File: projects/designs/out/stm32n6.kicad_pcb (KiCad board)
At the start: 2 copper layers, 89 parts, among them SW1 0R

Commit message: Update designs: add sub-block modules, board definition, layout, and KiCad exports
- Add charger (MCP73831), buck-boost (TPS63806), and LDO (LP5907) sub-block modules
- Add MCP73831 component definition
- Add stm32n6-board.sexp board definition with outline, rules, stackup, and zones
- Add stm32n6.layout with component placements and trace routing
- Mark optional ports on lt3045 module and stm32n6 ADC section
- Update BOM files with resolved component identities
- Add KiCad PCB exports for lt3045, power-6v, and tpsm84338
- Update stm32n6 KiCad PCB with traces, vias, and zone data
- Update footprint courtyard definitions

Co-Authored-By: Claude Opus 4.6 (1M context) <noreply@anthropic.com>
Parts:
- removed C1, C2, C21, C22, C23, C24, C25, C26, C27, C28, C29, C3, C30, C31, C32, C33, C34, C4, C5: 100nF, C_0201_0603Metric
- removed C10, C11, C12, C13, C14, C15, C16, C19, C20: 1uF, C_0201_0603Metric
- removed C17: 10uF, C_0603_1608Metric
- removed the C18 at (240.0, 0.00)
- removed the C18 at (180.0, 0.00)
- removed the C35 at (380.0, 0.00)
- removed the C35 at (-4.00, -2.00)
- removed C6, C7, C8, C9: 15uF, C_0603_1608Metric
- removed C_BOOT: 100nF, C_0402_1005Metric
- removed J2: , AMPHENOL_10164986-00011LF
- removed J3: , LSH02001GDAKTR
- removed L2: 0.47uH, l-1616
- removed R_FBB: 91k, R_0402_1005Metric
- removed R_FBT: 511k, R_0402_1005Metric
- removed R_PG: 100k, R_0402_1005Metric
- removed U1: , BGA223C50P19X19_1000X1000X100
- removed U2: , SON50P150X170X55-6N-D
- removed U4: , BGA24C100P5X5_600X800X120
- removed U7: , SOT95P280X145-5N
- removed Y1: , ABM810000MHZ12D2W
- removed Y2: , FC135327680KAAC3
- added C100: 100nF, C_0402_1005Metric, F.Cu at (93.2, 87.9)
- added C101: 10uF, C_0805_2012Metric, F.Cu at (84.2, 84.5)
- added C102: 1uF, C_0402_1005Metric, F.Cu at (79.1, 90.9)
- added C103: 1uF, C_0402_1005Metric, F.Cu at (81.9, 90.9)
- added C104: 330pF, C_0402_1005Metric, F.Cu at (84.7, 90.9)
- added C105: 330pF, C_0402_1005Metric, F.Cu at (87.5, 90.9)
- added C18: 2.2nF, C_0402_1005Metric, F.Cu at (41.0, 17.1)
- added C35: 100nF, C_0201_0603Metric, F.Cu at (25.6, 31.2)
- added C55: 1uF, C_0201_0603Metric, F.Cu at (35.2, 23.1)
- added C56: 100nF, C_0201_0603Metric, F.Cu at (37.6, 23.1)
- added C57: 100nF, C_0201_0603Metric, F.Cu at (40.0, 23.1)
- added C58: 100nF, C_0201_0603Metric, F.Cu at (23.2, 25.8)
- added C59: 100nF, C_0201_0603Metric, F.Cu at (28.0, 25.8)
- added C60: 100nF, C_0201_0603Metric, F.Cu at (30.4, 25.8)
- added C61: 100nF, C_0201_0603Metric, F.Cu at (32.8, 25.8)
- added C62: 100nF, C_0201_0603Metric, F.Cu at (35.2, 25.8)
- added C63: 100nF, C_0201_0603Metric, F.Cu at (37.6, 25.8)
- added C64: 100nF, C_0201_0603Metric, F.Cu at (40.0, 25.8)
- added C65: 100nF, C_0201_0603Metric, F.Cu at (23.2, 28.5)
- added C66: 100nF, C_0201_0603Metric, F.Cu at (25.6, 28.5)
- added C67: 100nF, C_0201_0603Metric, F.Cu at (28.0, 28.5)
- added C68: 100nF, C_0201_0603Metric, F.Cu at (30.4, 28.5)
- added C69: 100nF, C_0201_0603Metric, F.Cu at (32.8, 28.5)
- added C70: 100nF, C_0201_0603Metric, F.Cu at (35.2, 28.5)
- added C71: 1uF, C_0201_0603Metric, F.Cu at (37.6, 28.5)
- added C72: 4.7uF, C_0603_1608Metric, F.Cu at (31.9, 17.3)
- added C73: 1uF, C_0201_0603Metric, F.Cu at (41.5, 30.5)
- added C74: 100nF, C_0201_0603Metric, F.Cu at (23.2, 31.2)
- added C75: 10pF, C_0402_1005Metric, F.Cu at (88.4, 13.0)
- added C76: 10pF, C_0402_1005Metric, F.Cu at (91.2, 13.0)
- added C77: 6.8pF, C_0402_1005Metric, F.Cu at (114.1, 13.0)
- added C78: 6.8pF, C_0402_1005Metric, F.Cu at (116.9, 13.0)
- added C79: 100nF, C_0201_0603Metric, F.Cu at (64.2, 43.0)
- added C80: 100nF, C_0201_0603Metric, F.Cu at (63.2, 40.0)
- added C81: 100nF, C_0201_0603Metric, F.Cu at (67.2, 41.0)
- added C82: 100nF, C_0201_0603Metric, F.Cu at (72.8, 41.5)
- added C83: 100nF, C_0201_0603Metric, F.Cu at (70.2, 40.0)
- added C84: 100nF, C_0201_0603Metric, F.Cu at (27.5, 78.5)
- added C85: 100nF, C_0201_0603Metric, F.Cu at (25.0, 80.5)
- added C93: 10uF, C_0805_2012Metric, F.Cu at (86.1, 76.2)
- added C94: 10uF, C_0805_2012Metric, F.Cu at (90.5, 76.2)
- added C95: 100nF, C_0402_1005Metric, F.Cu at (81.9, 87.9)
- added C96: 100nF, C_0402_1005Metric, F.Cu at (84.7, 87.9)
- added C97: 100nF, C_0402_1005Metric, F.Cu at (87.6, 87.9)
- added C98: 100nF, C_0402_1005Metric, F.Cu at (90.4, 87.9)
- added C99: 10uF, C_0805_2012Metric, F.Cu at (79.8, 84.5)
- added FB1: 600R@100MHz, FB_0402_1005Metric, F.Cu at (25.0, 60.0)
- added FB2: 600R@100MHz, FB_0402_1005Metric, F.Cu at (30.0, 60.0)
- added FB3: 600R@100MHz, FB_0402_1005Metric, F.Cu at (35.0, 60.0)
- added FB4: 600R@100MHz, FB_0402_1005Metric, F.Cu at (37.0, 57.5)
- added FB5: 600R@100MHz, FB_0402_1005Metric, F.Cu at (45.0, 60.0)
- added H1: , A_Wurth_WA-SMSI_9774020633R, F.Cu at (108.1, 75.8)
- added H2: , A_Wurth_WA-SMSI_9774020633R, F.Cu at (115.0, 79.5)
- added R2: 10k, R_0201_0603Metric, F.Cu at (25.6, 25.8)
- added R22: 25R, R_0402_1005Metric, F.Cu at (87.9, 84.0)
- added R23: 25R, R_0402_1005Metric, F.Cu at (90.7, 84.0)
- added R24: 25R, R_0402_1005Metric, F.Cu at (93.6, 84.0)
- added R25: 25R, R_0402_1005Metric, F.Cu at (79.1, 87.9)
- added buck/C108: 10uF, C_0603_1608Metric, F.Cu at (46.8, 106.5)
- added buck/C109: 47uF, C_0805_2012Metric, F.Cu at (53.5, 105.8)
- added buck/C110: 47uF, C_0805_2012Metric, F.Cu at (51.5, 105.8)
- added buck/R28: 511k, R_0402_1005Metric, F.Cu at (49.5, 105.5)
- added buck/R29: 91k, R_0402_1005Metric, F.Cu at (49.5, 104.5)
- added buck/R30: 100k, R_0402_1005Metric, F.Cu at (48.0, 105.0)
- added buck/U12: , dsbga-15, F.Cu at (49.0, 107.0)
- added charger/C106: 4.7uF, C_0402_1005Metric, F.Cu at (23.5, 105.2)
- added charger/C107: 4.7uF, C_0402_1005Metric, F.Cu at (23.5, 109.0)
- added charger/R26: 2k, R_0402_1005Metric, F.Cu at (25.8, 105.2)
- added charger/R27: 1k, R_0402_1005Metric, F.Cu at (25.8, 110.0)
- added charger/U11: orange, LED_0402_1005Metric, F.Cu at (25.8, 109.0)
- added ldo/C111: 1uF, C_0402_1005Metric, F.Cu at (64.5, 94.5)
- added ldo/C112: 1uF, C_0402_1005Metric, F.Cu at (70.5, 94.5)
- added ldo/U14: , SOT95P280X145-5N, F.Cu at (67.5, 95.0)
- C36: value 4.7uF -> 100nF; footprint C_0402_1005Metric -> C_0201_0603Metric
- C37: value 1uF -> 100nF; footprint C_0402_1005Metric -> C_0201_0603Metric
- C38: footprint C_0402_1005Metric -> C_0201_0603Metric
- C39, C40: value 10pF -> 100nF; footprint C_0402_1005Metric -> C_0201_0603Metric
- C41, C42: value 6.8pF -> 15uF; footprint C_0805_2012Metric -> C_0603_1608Metric
- C43, C44: value 100nF -> 15uF; footprint C_0805_2012Metric -> C_0603_1608Metric
- C45, C46: value 100nF -> 1uF; footprint C_0805_2012Metric -> C_0201_0603Metric
- C47, C48, C49: value 100nF -> 1uF; footprint C_0402_1005Metric -> C_0201_0603Metric
- C50: value 10uF -> 1uF; footprint C_0402_1005Metric -> C_0201_0603Metric
- C51: value 47uF -> 1uF; footprint C_0402_1005Metric -> C_0201_0603Metric
- C52: value 47uF -> 10uF; footprint C_0402_1005Metric -> C_0603_1608Metric
- C53: value 1uF -> 10uF; footprint C_0805_2012Metric -> C_0603_1608Metric
- C54: footprint C_0805_2012Metric -> C_0201_0603Metric
- L1: footprint L_0805_2012Metric -> L_2016_Murata_DFE201610P
- R10, R11, R12, R13, R14, R8: footprint R_0402_1005Metric -> R_0201_0603Metric
- U3: footprint BGA24C100P5X5_800X600X120 -> BGA223C50P19X19_1000X1000X100
- U5: footprint QFN40P300X300X105-25N-D -> USB4510-03-1-A_GCT
- U6: footprint dsbga-15 -> BGA24C100P5X5_800X600X120
- moved C54 837.5 mm to (32.8, 23.1)
- moved C53 832.2 mm to (27.9, 17.3)
- moved C52 776.2 mm to (24.0, 17.3)
- moved C51 760.0 mm to (30.4, 23.1)
- moved C50 752.4 mm to (28.0, 23.1)
- moved C48 708.6 mm to (23.2, 23.1)
- moved U6 706.5 mm to (64.8, 42.0), turned to 180 degrees
- moved C49 704.9 mm to (25.6, 23.1)
- moved U5 702.8 mm to (29.0, 50.5)
- moved C47 651.3 mm to (40.0, 20.4)
- moved C46 650.7 mm to (37.6, 20.4)
- moved R12 649.8 mm to (71.8, 44.5), turned to 90 degrees
- moved D2 618.9 mm to (62.8, 44.5), turned to 270 degrees
- moved R11 605.2 mm to (66.2, 42.0)
- moved R10 597.9 mm to (63.8, 44.5), turned to 90 degrees
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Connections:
- C36 pad 1: V08CAP.U1.G1 -> VDD.U3.J14
- C37 pad 1: VREF+.U1.W2 -> VDD.U3.K14
- C38 pad 1: VREF+.U1.W2 -> VDD.U3.L14
- C39 pad 1: OSC_IN -> VDD.U3.F1
- C40 pad 1: OSC_OUT -> VDDA18AON.U3.H6
- C41 pad 1: OSC32_IN -> VDDCORE.U3.P7
- C42 pad 1: OSC32_OUT -> VDDCORE.U3.P7
- C43 pad 1: VDDIO3.U3.B4 -> VDDCORE.U3.P7
- C44 pad 1: VDDIO3.U3.E4 -> VDDCORE.U3.P7
- C45 pad 1: VDDIO3.U3.D1 -> VDDCORE.U3.G2
- C46 pad 1: VDDIO2.U4.D1 -> VDDCORE.U3.P7
- C47 pad 1: VDDIO2.U4.E4 -> VDDCORE.U3.P9
- C48 pad 1: VDD -> VDDCORE.U3.P10
- C49 pad 1: IMU_REGOUT -> VDDCORE.U3.P11
- C50 pad 1: VBATT.U6.VIN_1 -> VDDCORE.U3.P13
- C51 pad 1: VDD.U6.VOUT_1 -> VDDCORE.U3.W6
- C52 pad 1: VDD.U6.VOUT_1 -> VDD.U3.L1
- C53 pad 1: VDD.U7.IN -> VDD.U3.L1
- C54 pad 1: V1P8.U7.OUT -> VDD.U3.L1
- R10 pad 2: VDD -> V1P8
- R11 pad 2: VDD -> V1P8
- R12 pad 2: VDD -> V1P8
- U3 pad A4: FLASH_RESET -> (no net)
- U3 pad A5: (no net) -> OSC_IN
- U3 pad B2: FLASH_CLK -> (no net)
- U3 pad B3: GND -> (no net)
- U3 pad B4: VDDIO3.U3.B4 -> (no net)
- U3 pad B5: (no net) -> OSC_OUT
- U3 pad C1: GND -> USB_DP
- U3 pad C2: FLASH_NCS -> USB_DN
- U3 pad C3: FLASH_DQS -> VDD
- U3 pad D1: VDDIO3.U3.D1 -> OSC32_OUT
- U3 pad D2: FLASH_IO1 -> (no net)
- U3 pad D4: FLASH_IO3 -> VDDA18USB
- U3 pad D5: FLASH_IO4 -> (no net)
- U3 pad E1: FLASH_IO7 -> OSC32_IN
- U3 pad E2: FLASH_IO6 -> TXRTUNE
- U3 pad E4: VDDIO3.U3.E4 -> (no net)
- U5 pad 13: VDD -> (no net)
- U6 pad A2: VBATT -> (no net)
- U6 pad A3: VBATT -> (no net)
- U6 pad B1: GND -> (no net)
- U6 pad B2: SW_L1 -> FLASH_CLK
- U6 pad B3: SW_L1 -> GND
- U6 pad C2: GND -> FLASH_NCS
- U6 pad C3: GND -> FLASH_DQS
- U6 pad D1: FB_3V3 -> V1P8.U6.D1
- U6 pad D2: SW_L2 -> FLASH_IO1
- U6 pad D3: SW_L2 -> FLASH_IO0
- U6 pad E1: PG_3V3 -> FLASH_IO7
- U6 pad E2: VDD -> FLASH_IO6
- U6 pad E3: VDD -> FLASH_IO5
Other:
- board outline added: 12.2 x 6.7 mm

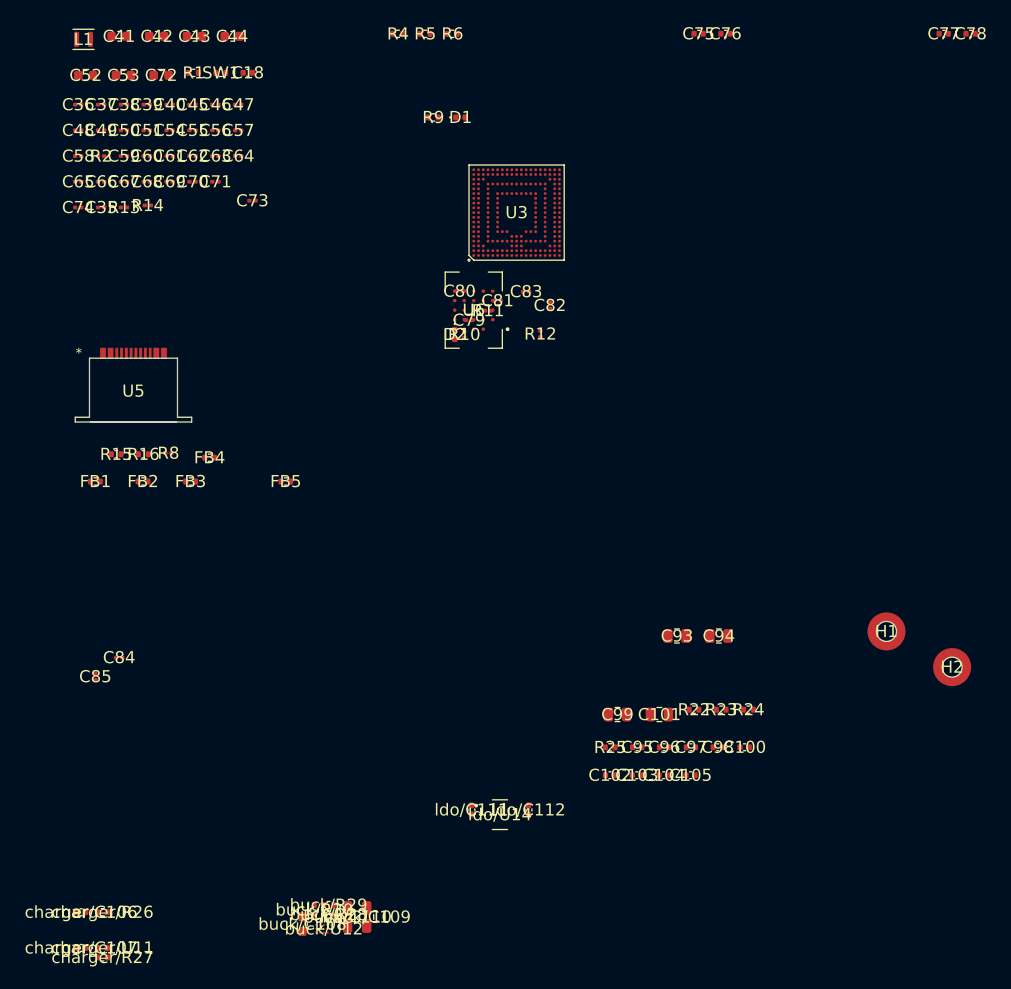
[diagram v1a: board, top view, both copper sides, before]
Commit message: Update designs: add BOMs, layouts, and 2049280301 connector library
Regenerate stm32n6 BOM/layout, refresh board definition and exported
.kicad_pcb. Add new BOMs (board, concept-example, som-h563) and
pma3-14ln layout. Add .kicad.json sync config for stm32n6.

Import Molex 204928-0301 symbol/footprint/3D model into lib/sources/.

Co-Authored-By: Claude Opus 4.7 (1M context) <noreply@anthropic.com>
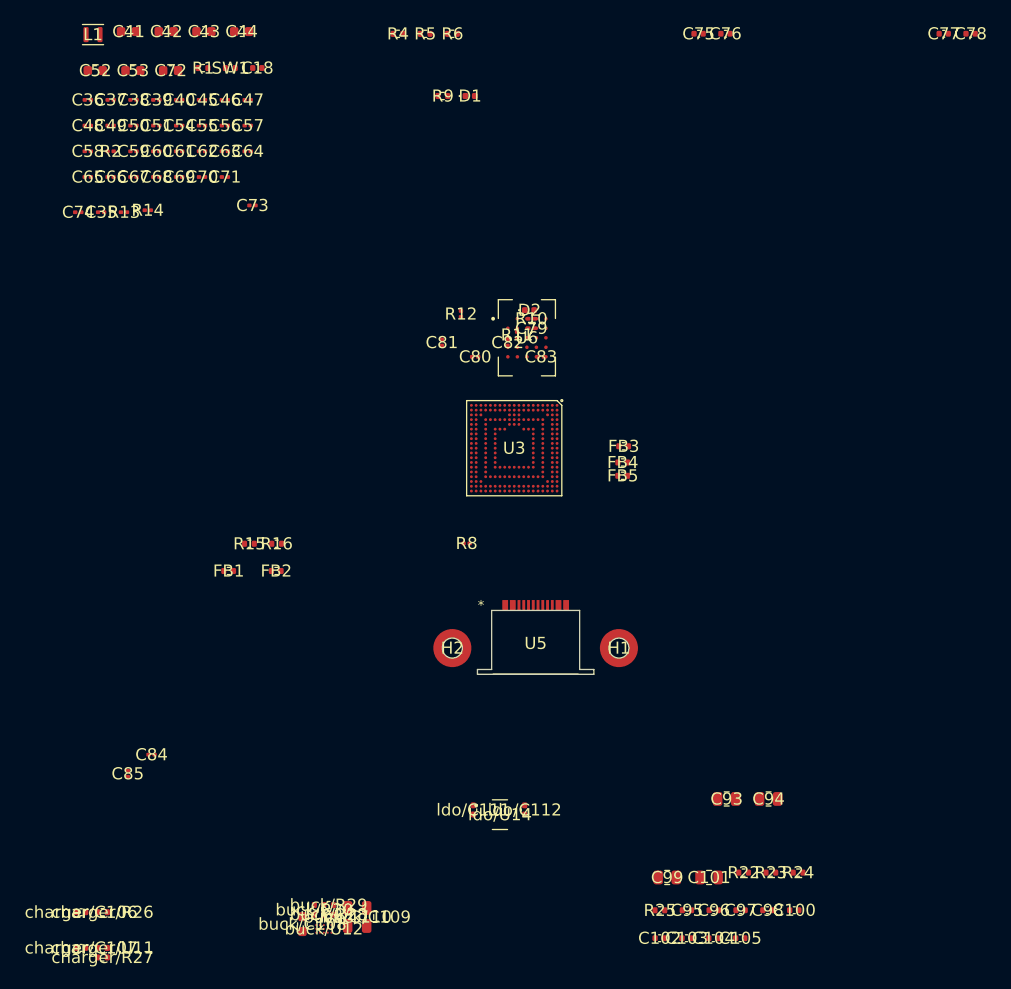
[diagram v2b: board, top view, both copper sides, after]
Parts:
- moved H2 52.5 mm to (62.5, 77.5)
- moved U5 49.9 mm to (71.2, 77.0)
- moved FB3 45.7 mm to (80.5, 56.3)
- moved FB4 43.4 mm to (80.4, 58.0)
- moved FB5 35.4 mm to (80.4, 59.4)
- moved R8 32.7 mm to (64.0, 66.5)
- moved H1 28.2 mm to (80.0, 77.5)
- moved U3 24.8 mm to (69.0, 56.5), turned to 270 degrees
- moved C100 17.9 mm to (98.4, 105.0)
- moved C102 17.9 mm to (84.3, 108.0)
- moved C103 17.9 mm to (87.1, 108.0)
- moved C104 17.9 mm to (89.9, 108.0)
- moved C105 17.9 mm to (92.7, 108.0)
- moved C95 17.9 mm to (87.1, 105.0)
- moved C96 17.9 mm to (90.0, 105.0)
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
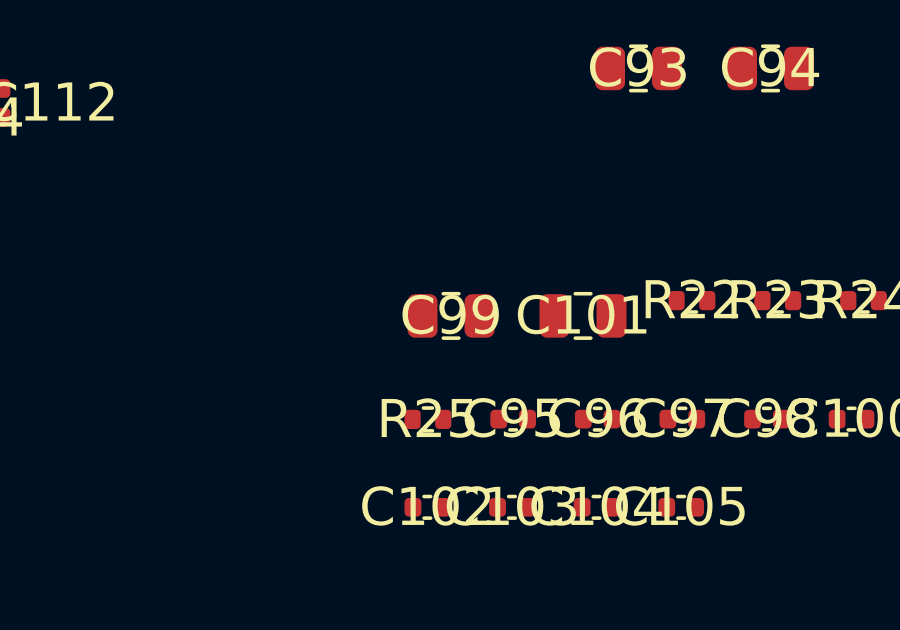
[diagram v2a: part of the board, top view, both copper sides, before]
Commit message: Add RF switch design, new component libraries, history snapshots
- New design: rf-switch-8way (sexp + BOM)
- Library additions: AD7380-4, PE42582, GRF1-J-P-08, TPS60150, USB
  connectors (4130-GF-C, 4235-03-C), APTF1616, 204928-0301 connector,
  SMA-J-P-H-ST, testpoint, battery wire pad — symbols, footprints,
  pinouts, and STEP models.
- Existing design updates: stm32n6 sexp/layout/BOM, lt3045/power-6v/
  tpsm84338 BOM refreshes, kicad_pcb regen, board.sexp removed.
- History snapshots for stm32n6 edits.

Co-Authored-By: Claude Opus 4.7 (1M context) <noreply@anthropic.com>
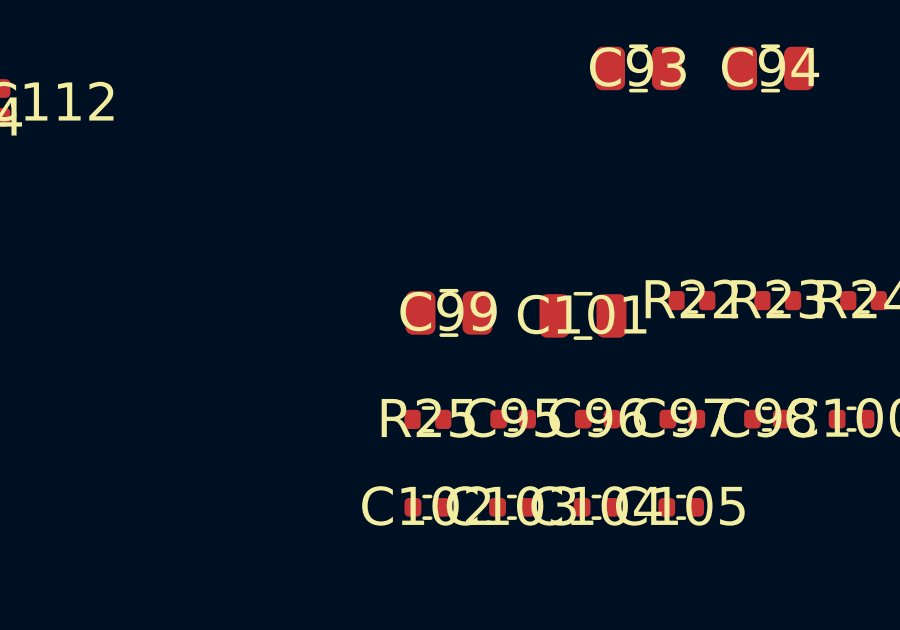
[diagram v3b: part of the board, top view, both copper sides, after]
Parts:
- moved C99 0.12 mm to (85.0, 101.5)
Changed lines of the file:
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@@
 	(footprint "C_0805_2012Metric"
 		(layer "F.Cu")
-		(at 85.07 101.60)
+		(at 85.00 101.50)
 		(descr "Capacitor SMD 0805 (2012 Metric), square (rectangular) end terminal, IPC-7351 nominal")
 		(property "Reference" "C99"
